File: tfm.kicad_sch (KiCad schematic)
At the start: 36 parts, among them J1 Screw_Terminal_01x04, J2 Screw_Terminal_01x04, J3 Conn_01x03, J4 Conn_01x03, J5 Conn_01x03, J7 Conn_02x04_Counter_Clockwise, J8 Conn_01x02_Female, U1 LPS25HB, U2 SHT40, U3 NCP1117-3.3_SOT223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

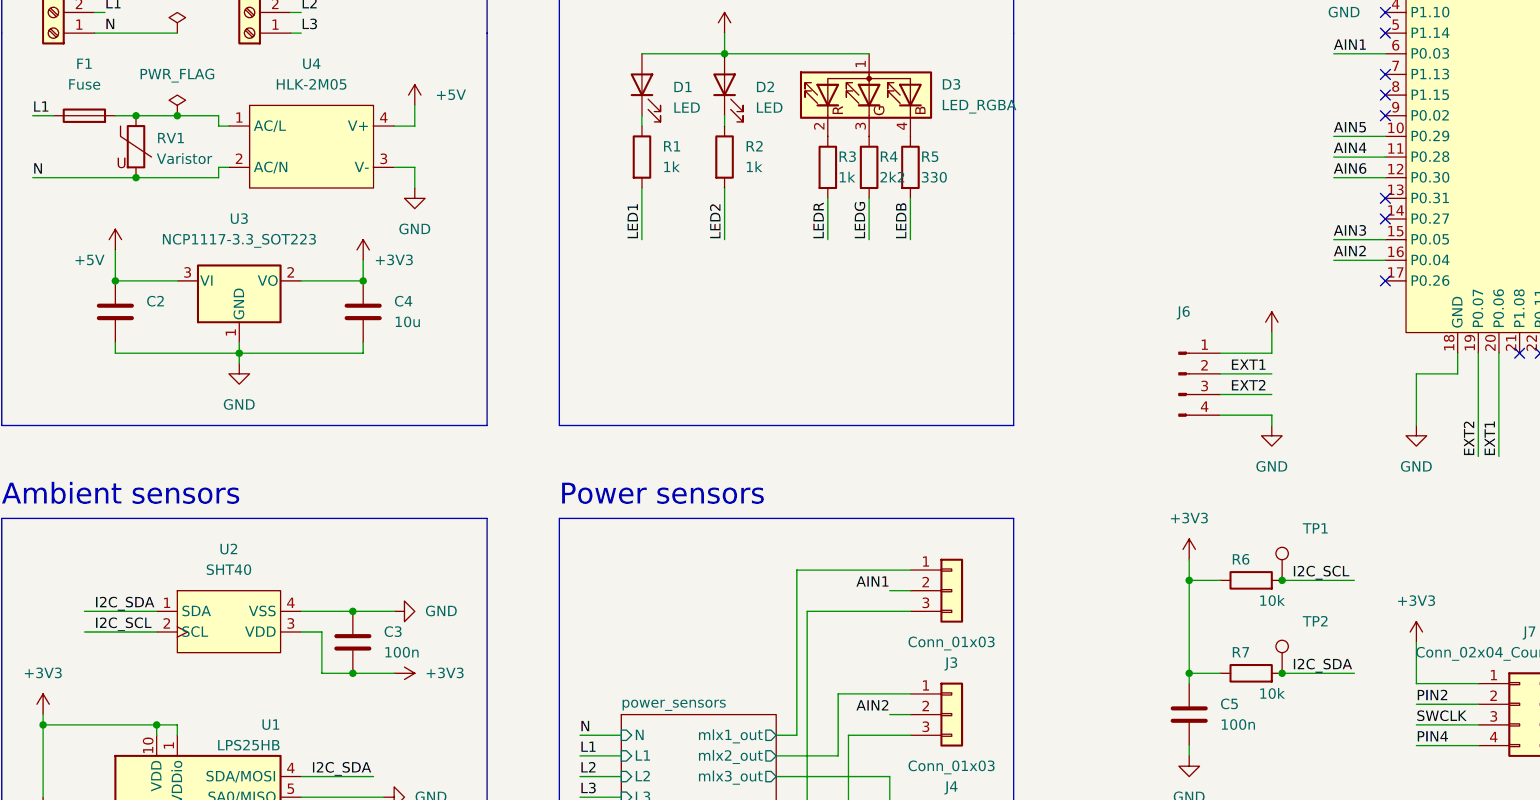
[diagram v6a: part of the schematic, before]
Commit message: Fix divider and leds after board tested
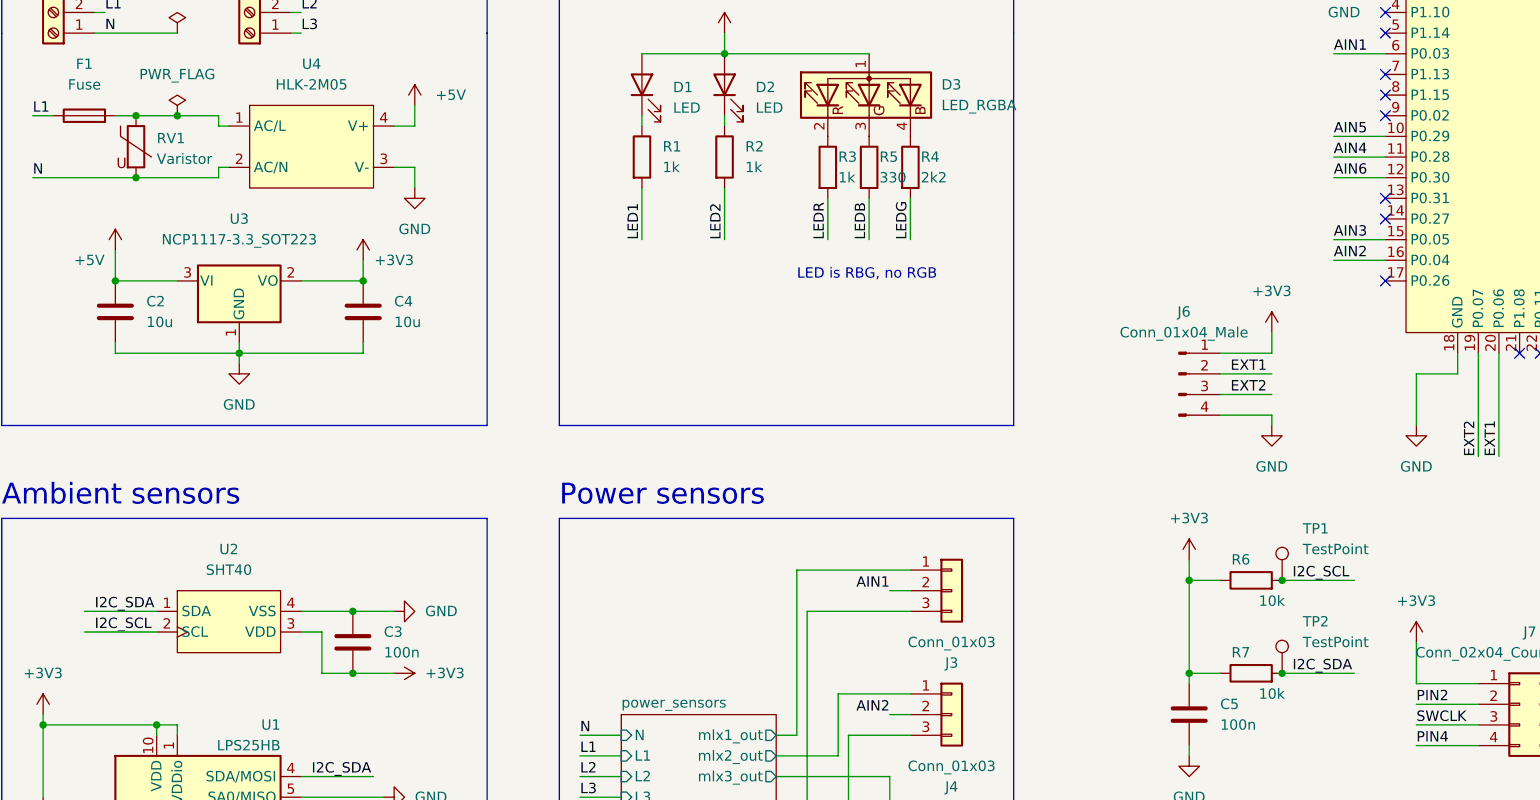
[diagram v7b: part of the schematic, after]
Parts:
- C2: value (none) -> 10u; footprint (none) -> Capacitor_SMD:C_1206_3216Metric
- C4: footprint (none) -> Capacitor_SMD:C_1206_3216Metric
- J6: value (none) -> Conn_01x04_Male; footprint (none) -> Connector_PinHeader_2.54mm:PinHeader_1x04_P2.54mm_Vertical
- TP1, TP2: value (none) -> TestPoint; footprint (none) -> TestPoint:TestPoint_Pad_D1.5mm
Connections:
- net at R4.1: now also D3.4 (BK); no longer D3.3 (GK)
- net at R5.1: now also D3.3 (GK); no longer D3.4 (BK)
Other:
- note added: "LED is RBG, no RGB"
- moved on the sheet: R4, R5

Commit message: Last Power Meter 1.0 commit
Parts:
- C6, C7: value 330p -> 100p
- R1, R2: value 1k -> 2k2
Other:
- note added: "Enviroment sensors"
- note removed: "Ambient sensors"
- moved on the sheet: C6, D1, D2, D3, R1, R2, R3, R4, R5, TP3, TP4
